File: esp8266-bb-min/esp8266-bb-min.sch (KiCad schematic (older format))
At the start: 14 parts, among them J1 Conn_01x02_Male, J2 Conn_02x08_Odd_Even, U1 tps77633d-SOIC8, U2 ESP-12F

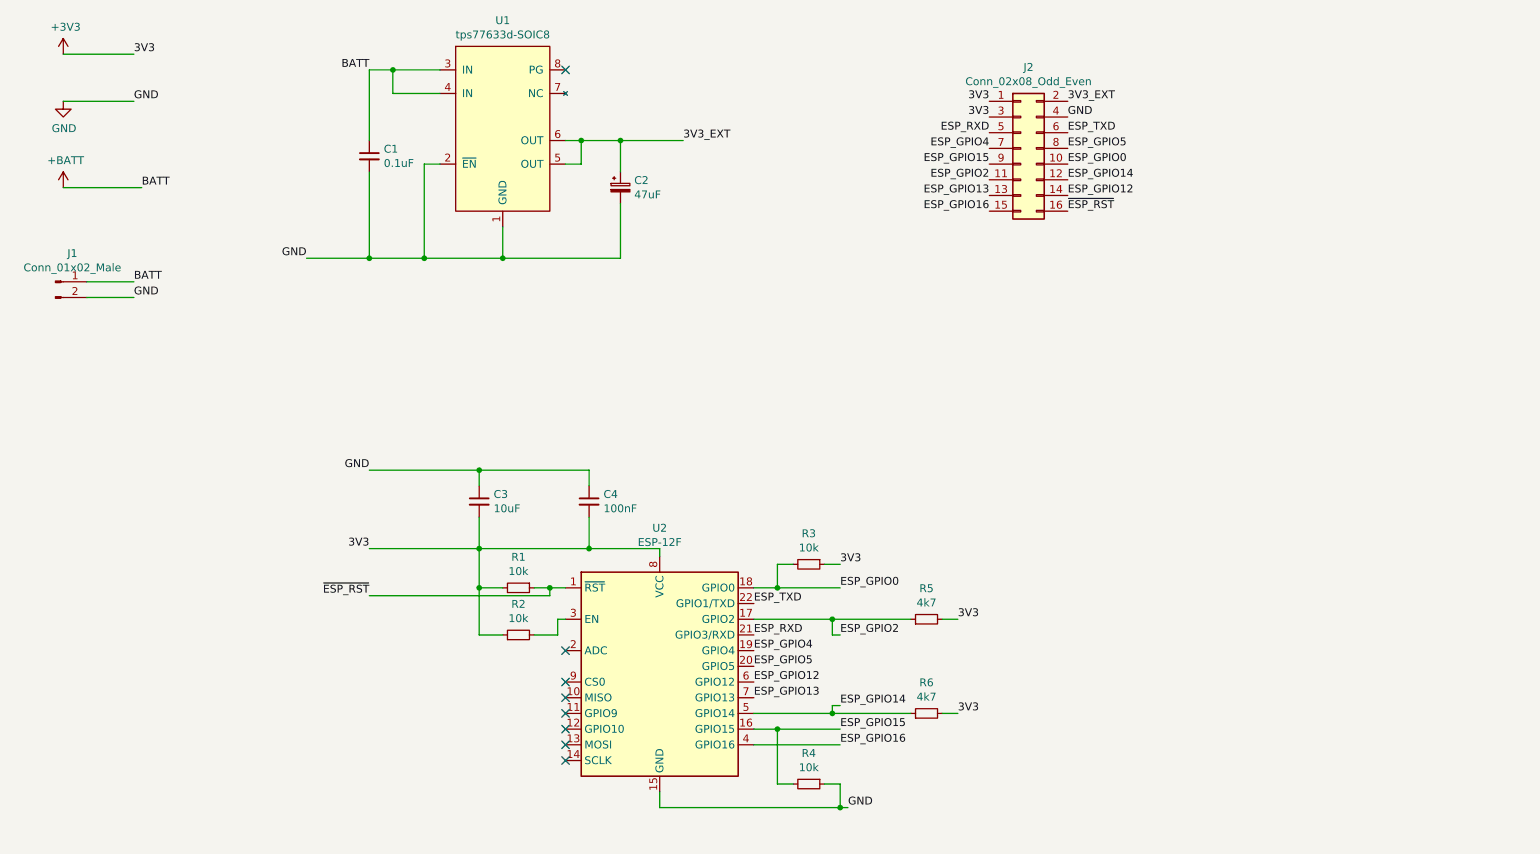
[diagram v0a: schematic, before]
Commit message: *: cleanup of erc errors
Signed-off-by: Dominik Laton <dominik.laton@web.de>
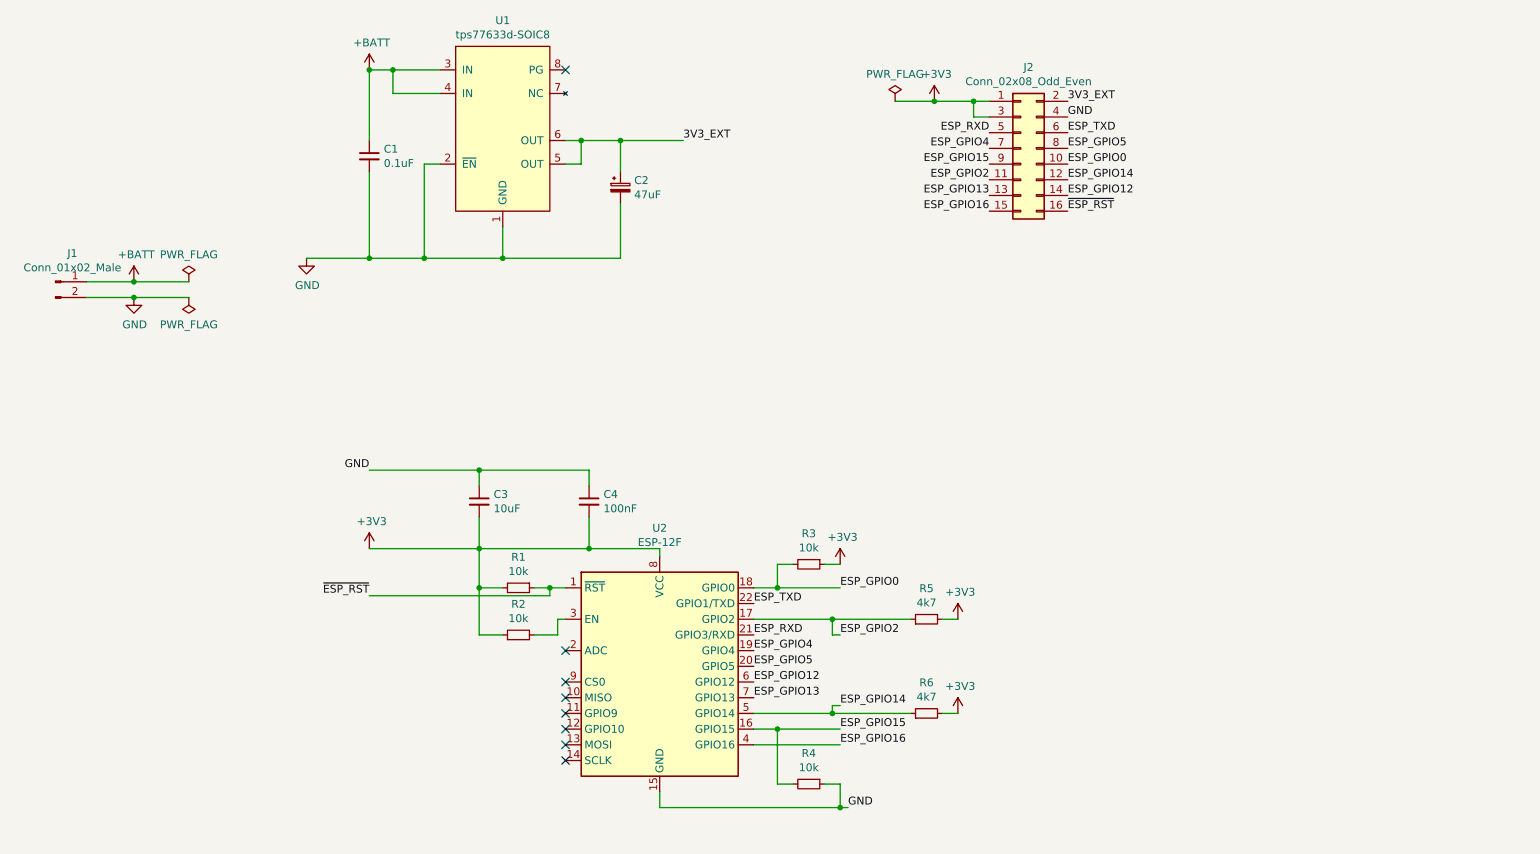
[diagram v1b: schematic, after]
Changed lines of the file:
@@
 L power:+3V3 #PWR0101
 U 1 1 5FA21016
-P 1050 850
-F 0 "#PWR0101" H 1050 700 50  0001 C CNN
-F 1 "+3V3" H 1065 1023 50  0000 C CNN
-F 2 "" H 1050 850 50  0001 C CNN
-F 3 "" H 1050 850 50  0001 C CNN
-	1    1050 850
+P 6600 1150
+F 0 "#PWR0101" H 6600 1000 50  0001 C CNN
+F 1 "+3V3" H 6615 1323 50  0000 C CNN
+F 2 "" H 6600 1150 50  0001 C CNN
+F 3 "" H 6600 1150 50  0001 C CNN
+	1    6600 1150
 	1    0    0    -1
 $EndComp
@@
 L power:GND #PWR0102
 U 1 1 5FA2192E
-P 1050 1150
-F 0 "#PWR0102" H 1050 900 50  0001 C CNN
-F 1 "GND" H 1055 977 50  0000 C CNN
-F 2 "" H 1050 1150 50  0001 C CNN
-F 3 "" H 1050 1150 50  0001 C CNN
-	1    1050 1150
+P 1500 2400
+F 0 "#PWR0102" H 1500 2150 50  0001 C CNN
+F 1 "GND" H 1505 2227 50  0000 C CNN
+F 2 "" H 1500 2400 50  0001 C CNN
+F 3 "" H 1500 2400 50  0001 C CNN
+	1    1500 2400
 	1    0    0    -1
 $EndComp
@@
 L power:+BATT #PWR0103
 U 1 1 5FA21D4E
-P 1050 1700
-F 0 "#PWR0103" H 1050 1550 50  0001 C CNN
-F 1 "+BATT" H 1065 1873 50  0000 C CNN
-F 2 "" H 1050 1700 50  0001 C CNN
-F 3 "" H 1050 1700 50  0001 C CNN
-	1    1050 1700
+P 1500 2300
+F 0 "#PWR0103" H 1500 2150 50  0001 C CNN
+F 1 "+BATT" H 1515 2473 50  0000 C CNN
+F 2 "" H 1500 2300 50  0001 C CNN
+F 3 "" H 1500 2300 50  0001 C CNN
+	1    1500 2300
 	1    0    0    -1
 $EndComp
@@
 Wire Wire Line
 	1200 2300 1500 2300
-Text Label 1500 2300 0    50   ~ 0
-BATT
-Wire Wire Line
-	1050 1700 1550 1700
-Text Label 1550 1700 0    50   ~ 0
-BATT
-Wire Wire Line
-	1050 1150 1500 1150
-Text Label 1500 1150 0    50   ~ 0
-GND
 Wire Wire Line
 	1200 2400 1500 2400
-Text Label 1500 2400 0    50   ~ 0
-GND
-Wire Wire Line
-	1050 850  1500 850
-Text Label 1500 850  0    50   ~ 0
-3V3
 Text Label 7450 1150 0    50   ~ 0
 3V3_EXT
-Text Label 6950 1150 2    50   ~ 0
-3V3
 $Comp
 L domi3006:tps77633d-SOIC8 U1
@@
 Wire Wire Line
 	3150 950  3000 950
-Text Label 3000 950  2    50   ~ 0
-BATT
 Wire Wire Line
 	3450 1550 3350 1550
@@
 	3350 2150 3000 2150
 Connection ~ 3350 2150
-Text Label 2600 2150 2    50   ~ 0
-GND
 $Comp
 L Device:C_Small C1
@@
 Wire Wire Line
 	4850 4000 4400 4000
-Text Label 3000 4000 2    50   ~ 0
-3V3
 $Comp
 L Device:R_Small R1
@@
 Wire Wire Line
 	5900 4100 6000 4100
-Text Label 6000 4100 0    50   ~ 0
-3V3
 Text Label 6000 4250 0    50   ~ 0
 ESP_GPIO0
@@
 Text Label 6950 1850 2    50   ~ 0
 ESP_GPIO16
-Text Label 6950 1250 2    50   ~ 0
-3V3
 Text Label 7450 1250 0    50   ~ 0
 GND
@@
 Wire Wire Line
 	6650 5050 6750 5050
-Text Label 6750 5050 0    50   ~ 0
-3V3
-Text Label 6750 4450 0    50   ~ 0
-3V3
+$Comp
+L power:+BATT #PWR0104
+U 1 1 5FA5E5E8
+P 3000 950
+F 0 "#PWR0104" H 3000 800 50  0001 C CNN
+F 1 "+BATT" H 3015 1123 50  0000 C CNN
+F 2 "" H 3000 950 50  0001 C CNN
+F 3 "" H 3000 950 50  0001 C CNN
+	1    3000 950
+	1    0    0    -1
+$EndComp
+Connection ~ 3000 950
+Wire Wire Line
+	6950 1150 6850 1150
+$Comp
+L power:+3V3 #PWR0105
+U 1 1 5FA6F2A6
+P 3000 4000
+F 0 "#PWR0105" H 3000 3850 50  0001 C CNN
+F 1 "+3V3" H 3015 4173 50  0000 C CNN
+F 2 "" H 3000 4000 50  0001 C CNN
+F 3 "" H 3000 4000 50  0001 C CNN
+	1    3000 4000
+	1    0    0    -1
+$EndComp
+$Comp
+L power:GND #PWR0106
+U 1 1 5FA72AF4
+P 2600 2150
+F 0 "#PWR0106" H 2600 1900 50  0001 C CNN
+F 1 "GND" H 2605 1977 50  0000 C CNN
+F 2 "" H 2600 2150 50  0001 C CNN
+F 3 "" H 2600 2150 50  0001 C CNN
+	1    2600 2150
+	1    0    0    -1
+$EndComp
+$Comp
+L power:PWR_FLAG #FLG0101
+U 1 1 5FA7DBB5
+P 6350 1150
+F 0 "#FLG0101" H 6350 1225 50  0001 C CNN
+F 1 "PWR_FLAG" H 6350 1323 50  0000 C CNN
+F 2 "" H 6350 1150 50  0001 C CNN
+F 3 "~" H 6350 1150 50  0001 C CNN
+	1    6350 1150
+	1    0    0    -1
+$EndComp
+Wire Wire Line
+	6350 1150 6600 1150
+Connection ~ 6600 1150
+$Comp
+L power:PWR_FLAG #FLG0102
+U 1 1 5FA82854
+P 1850 2300
+F 0 "#FLG0102" H 1850 2375 50  0001 C CNN
+F 1 "PWR_FLAG" H 1850 2473 50  0000 C CNN
+F 2 "" H 1850 2300 50  0001 C CNN
+F 3 "~" H 1850 2300 50  0001 C CNN
+	1    1850 2300
+	1    0    0    -1
+$EndComp
+Wire Wire Line
+	1500 2300 1850 2300
+Connection ~ 1500 2300
+$Comp
+L power:PWR_FLAG #FLG0103
+U 1 1 5FA8A406
+P 1850 2400
+F 0 "#FLG0103" H 1850 2475 50  0001 C CNN
+F 1 "PWR_FLAG" H 1850 2573 50  0000 C CNN
+F 2 "" H 1850 2400 50  0001 C CNN
+F 3 "~" H 1850 2400 50  0001 C CNN
+	1    1850 2400
+	-1   0    0    1
+$EndComp
+Wire Wire Line
+	1500 2400 1850 2400
+Connection ~ 1500 2400
+Wire Wire Line
+	6850 1150 6850 1250
+Wire Wire Line
+	6850 1250 6950 1250
+Connection ~ 6850 1150
+Wire Wire Line
+	6850 1150 6600 1150
+$Comp
+L power:+3V3 #PWR?
+U 1 1 5FA98897
+P 6750 4450
+F 0 "#PWR?" H 6750 4300 50  0001 C CNN
+F 1 "+3V3" H 6765 4623 50  0000 C CNN
+F 2 "" H 6750 4450 50  0001 C CNN
+F 3 "" H 6750 4450 50  0001 C CNN
+	1    6750 4450
+	1    0    0    -1
+$EndComp
+$Comp
+L power:+3V3 #PWR?
+U 1 1 5FA997BF
+P 6750 5050
+F 0 "#PWR?" H 6750 4900 50  0001 C CNN
+F 1 "+3V3" H 6765 5223 50  0000 C CNN
+F 2 "" H 6750 5050 50  0001 C CNN
+F 3 "" H 6750 5050 50  0001 C CNN
+	1    6750 5050
+	1    0    0    -1
+$EndComp
+$Comp
+L power:+3V3 #PWR?
+U 1 1 5FA99D69
+P 6000 4100
+F 0 "#PWR?" H 6000 3950 50  0001 C CNN
+F 1 "+3V3" H 6015 4273 50  0000 C CNN
+F 2 "" H 6000 4100 50  0001 C CNN
+F 3 "" H 6000 4100 50  0001 C CNN
+	1    6000 4100
+	1    0    0    -1
+$EndComp
 $EndSCHEMATC

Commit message: sch: addressed issue domi3006/esp8266-bb-min#3
Signed-off-by: Dominik Laton <dominik.laton@web.de>
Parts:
- removed U1: tps77633d-SOIC8, domi3006:SOIC-8, symbol domi3006:tps77633d-SOIC8
- added R7: 56k, Resistor_SMD:R_0805_2012Metric_Pad1.20x1.40mm_HandSolder, symbol Device:R_Small
- added U1: LP38693MP-3.3, Package_TO_SOT_SMD:SOT-223-5, symbol Regulator_Linear:LP38693MP-3.3
- C1: value 0.1uF -> 1uF
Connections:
- net +3V3: now also C2.1, U1.3 (OUT)
- net +BATT: now also R7.2, U1.1 (EN), U1.4 (IN)
- net 3V3_EXT: no longer names the net of J2.2 (Pin_2)
- net 3V3_EXT: no longer C2.1
- net GND renamed -BATT
- net -BATT: now also R7.1, U1.5 (GND)
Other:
- note added: "-BATT and GND should meet at ldo\nC1 should be placed near to IN (max. 1cm)"
- moved on the sheet: C1
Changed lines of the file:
@@
-$EndComp
-$Comp
-L power:GND #PWR0102
-U 1 1 5FA2192E
-P 1500 2400
-F 0 "#PWR0102" H 1500 2150 50  0001 C CNN
-F 1 "GND" H 1505 2227 50  0000 C CNN
-F 2 "" H 1500 2400 50  0001 C CNN
-F 3 "" H 1500 2400 50  0001 C CNN
-	1    1500 2400
-	1    0    0    -1
 $EndComp
 $Comp
@@
 Wire Wire Line
 	1200 2300 1500 2300
-Wire Wire Line
-	1200 2400 1500 2400
-Text Label 7450 1150 0    50   ~ 0
-3V3_EXT
-$Comp
-L domi3006:tps77633d-SOIC8 U1
-U 1 1 5FA2A8A4
-P 3850 800
-F 0 "U1" H 3850 965 50  0000 C CNN
-F 1 "tps77633d-SOIC8" H 3850 874 50  0000 C CNN
-F 2 "domi3006:SOIC-8" H 3850 850 50  0001 C CNN
-F 3 "" H 3850 850 50  0001 C CNN
-	1    3850 800
-	1    0    0    -1
-$EndComp
-Wire Wire Line
-	3450 950  3150 950
-Wire Wire Line
-	3450 1100 3150 1100
-Wire Wire Line
-	3150 1100 3150 950
-Connection ~ 3150 950
-Wire Wire Line
-	3150 950  3000 950
-Wire Wire Line
-	3450 1550 3350 1550
-Wire Wire Line
-	3350 1550 3350 2150
-Wire Wire Line
-	3350 2150 3850 2150
-Wire Wire Line
-	3850 2150 3850 1950
-Wire Wire Line
-	3350 2150 3000 2150
-Connection ~ 3350 2150
 $Comp
 L Device:C_Small C1
 U 1 1 5FA2D191
-P 3000 1500
-F 0 "C1" H 3092 1546 50  0000 L CNN
-F 1 "0.1uF" H 3092 1455 50  0000 L CNN
-F 2 "Capacitor_SMD:C_0805_2012Metric_Pad1.18x1.45mm_HandSolder" H 3000 1500 50  0001 C CNN
-F 3 "~" H 3000 1500 50  0001 C CNN
-	1    3000 1500
-	1    0    0    -1
-$EndComp
-Wire Wire Line
-	3000 1600 3000 2150
-Connection ~ 3000 2150
-Wire Wire Line
-	3000 2150 2600 2150
-Wire Wire Line
-	3000 1400 3000 950
-NoConn ~ 4250 950
-Wire Wire Line
-	4250 1400 4350 1400
-Wire Wire Line
-	4250 1550 4350 1550
-Wire Wire Line
-	4350 1550 4350 1400
-Connection ~ 4350 1400
-Wire Wire Line
-	4350 1400 4600 1400
-Text Label 5000 1400 0    50   ~ 0
-3V3_EXT
+P 3000 1750
+F 0 "C1" H 3092 1796 50  0000 L CNN
+F 1 "1uF" H 3092 1705 50  0000 L CNN
+F 2 "Capacitor_SMD:C_0805_2012Metric_Pad1.18x1.45mm_HandSolder" H 3000 1750 50  0001 C CNN
+F 3 "~" H 3000 1750 50  0001 C CNN
+	1    3000 1750
+	1    0    0    -1
+$EndComp
 $Comp
 L Device:CP_Small C2
@@
 $EndComp
 Wire Wire Line
-	3850 2150 4600 2150
-Wire Wire Line
 	4600 2150 4600 1800
-Connection ~ 3850 2150
 Wire Wire Line
 	4600 1600 4600 1400
-Connection ~ 4600 1400
-Wire Wire Line
-	4600 1400 5000 1400
 Wire Wire Line
 	4850 4050 4850 4000
@@
 L power:+BATT #PWR0104
 U 1 1 5FA5E5E8
-P 3000 950
-F 0 "#PWR0104" H 3000 800 50  0001 C CNN
-F 1 "+BATT" H 3015 1123 50  0000 C CNN
-F 2 "" H 3000 950 50  0001 C CNN
-F 3 "" H 3000 950 50  0001 C CNN
-	1    3000 950
-	1    0    0    -1
-$EndComp
-Connection ~ 3000 950
+P 2750 1400
+F 0 "#PWR0104" H 2750 1250 50  0001 C CNN
+F 1 "+BATT" H 2765 1573 50  0000 C CNN
+F 2 "" H 2750 1400 50  0001 C CNN
+F 3 "" H 2750 1400 50  0001 C CNN
+	1    2750 1400
+	1    0    0    -1
+$EndComp
 Wire Wire Line
 	6950 1150 6850 1150
@@
 	1    0    0    -1
 $EndComp
-$Comp
-L power:GND #PWR0106
-U 1 1 5FA72AF4
-P 2600 2150
-F 0 "#PWR0106" H 2600 1900 50  0001 C CNN
-F 1 "GND" H 2605 1977 50  0000 C CNN
-F 2 "" H 2600 2150 50  0001 C CNN
-F 3 "" H 2600 2150 50  0001 C CNN
-	1    2600 2150
-	1    0    0    -1
-$EndComp
-$Comp
-L power:PWR_FLAG #FLG0101
-U 1 1 5FA7DBB5
-P 6350 1150
-F 0 "#FLG0101" H 6350 1225 50  0001 C CNN
-F 1 "PWR_FLAG" H 6350 1323 50  0000 C CNN
-F 2 "" H 6350 1150 50  0001 C CNN
-F 3 "~" H 6350 1150 50  0001 C CNN
-	1    6350 1150
-	1    0    0    -1
-$EndComp
-Wire Wire Line
-	6350 1150 6600 1150
-Connection ~ 6600 1150
 $Comp
 L power:PWR_FLAG #FLG0102
@@
 $EndComp
 Wire Wire Line
-	1500 2400 1850 2400
-Connection ~ 1500 2400
-Wire Wire Line
 	6850 1150 6850 1250
 Wire Wire Line
@@
 	6850 1150 6600 1150
 $Comp
-L power:+3V3 #PWR?
+L power:+3V3 #PWR0102
 U 1 1 5FA98897
 P 6750 4450
-F 0 "#PWR?" H 6750 4300 50  0001 C CNN
+F 0 "#PWR0102" H 6750 4300 50  0001 C CNN
 F 1 "+3V3" H 6765 4623 50  0000 C CNN
 F 2 "" H 6750 4450 50  0001 C CNN
@@
 $EndComp
 $Comp
-L power:+3V3 #PWR?
+L power:+3V3 #PWR0106
 U 1 1 5FA997BF
 P 6750 5050
-F 0 "#PWR?" H 6750 4900 50  0001 C CNN
+F 0 "#PWR0106" H 6750 4900 50  0001 C CNN
 F 1 "+3V3" H 6765 5223 50  0000 C CNN
 F 2 "" H 6750 5050 50  0001 C CNN
@@
 $EndComp
 $Comp
-L power:+3V3 #PWR?
+L power:+3V3 #PWR0107
 U 1 1 5FA99D69
 P 6000 4100
-F 0 "#PWR?" H 6000 3950 50  0001 C CNN
+F 0 "#PWR0107" H 6000 3950 50  0001 C CNN
 F 1 "+3V3" H 6015 4273 50  0000 C CNN
 F 2 "" H 6000 4100 50  0001 C CNN
@@
 	1    0    0    -1
 $EndComp
+$Comp
+L Regulator_Linear:LP38693MP-3.3 U1
+U 1 1 5FC250F2
+P 4000 1500
+F 0 "U1" H 4000 1842 50  0000 C CNN
+F 1 "LP38693MP-3.3" H 4000 1751 50  0000 C CNN
+F 2 "Package_TO_SOT_SMD:SOT-223-5" H 4000 1500 50  0001 C CNN
+F 3 "https://www.ti.com/lit/ds/symlink/lp38693.pdf" H 4000 1500 50  0001 C CNN
+	1    4000 1500
+	1    0    0    -1
+$EndComp
+Wire Wire Line
+	4400 1400 4600 1400
+Wire Wire Line
+	3000 1850 3000 2150
+Wire Wire Line
+	3600 1400 3400 1400
+Wire Wire Line
+	3000 1400 3000 1650
+Wire Wire Line
+	3000 2150 3400 2150
+Wire Wire Line
+	4000 1800 4000 2150
+Connection ~ 4000 2150
+Wire Wire Line
+	4000 2150 4600 2150
+Wire Wire Line
+	4600 2150 4600 2250
+Connection ~ 4600 2150
+$Comp
+L power:GND #PWR0108
+U 1 1 5FC3E3A8
+P 4600 2250
+F 0 "#PWR0108" H 4600 2000 50  0001 C CNN
+F 1 "GND" H 4605 2077 50  0000 C CNN
+F 2 "" H 4600 2250 50  0001 C CNN
+F 3 "" H 4600 2250 50  0001 C CNN
+	1    4600 2250
+	1    0    0    -1
+$EndComp
+$Comp
+L power:-BATT #PWR0109
+U 1 1 5FC40056
+P 2750 2150
+F 0 "#PWR0109" H 2750 2000 50  0001 C CNN
+F 1 "-BATT" H 2765 2323 50  0000 C CNN
+F 2 "" H 2750 2150 50  0001 C CNN
+F 3 "" H 2750 2150 50  0001 C CNN
+	1    2750 2150
+	1    0    0    -1
+$EndComp
+Wire Wire Line
+	2750 2150 3000 2150
+Connection ~ 3000 2150
+Wire Wire Line
+	2750 1400 3000 1400
+Connection ~ 3000 1400
+$Comp
+L Device:R_Small R7
+U 1 1 5FC4664C
+P 3400 1750
+F 0 "R7" V 3204 1750 50  0000 C CNN
+F 1 "56k" V 3295 1750 50  0000 C CNN
+F 2 "Resistor_SMD:R_0805_2012Metric_Pad1.20x1.40mm_HandSolder" H 3400 1750 50  0001 C CNN
+F 3 "~" H 3400 1750 50  0001 C CNN
+	1    3400 1750
+	-1   0    0    1
+$EndComp
+Wire Wire Line
+	3600 1500 3400 1500
+Wire Wire Line
+	3400 1500 3400 1400
+Connection ~ 3400 1400
+Wire Wire Line
+	3400 1400 3000 1400
+Wire Wire Line
+	3400 1500 3400 1650
+Connection ~ 3400 1500
+Wire Wire Line
+	3400 1850 3400 2150
+Connection ~ 3400 2150
+Wire Wire Line
+	3400 2150 4000 2150
+$Comp
+L power:+3.3V #PWR0110
+U 1 1 5FC51A47
+P 4800 1400
+F 0 "#PWR0110" H 4800 1250 50  0001 C CNN
+F 1 "+3.3V" H 4815 1573 50  0000 C CNN
+F 2 "" H 4800 1400 50  0001 C CNN
+F 3 "" H 4800 1400 50  0001 C CNN
+	1    4800 1400
+	1    0    0    -1
+$EndComp
+Wire Wire Line
+	4600 1400 4800 1400
+Connection ~ 4600 1400
+NoConn ~ 7450 1150
+Wire Wire Line
+	1200 2400 1650 2400
+$Comp
+L power:-BATT #PWR0111
+U 1 1 5FC561B1
+P 1650 2400
+F 0 "#PWR0111" H 1650 2250 50  0001 C CNN
+F 1 "-BATT" H 1665 2573 50  0000 C CNN
+F 2 "" H 1650 2400 50  0001 C CNN
+F 3 "" H 1650 2400 50  0001 C CNN
+	1    1650 2400
+	1    0    0    -1
+$EndComp
+Connection ~ 1650 2400
+Wire Wire Line
+	1650 2400 1850 2400
+Text Notes 2700 2350 0    50   ~ 0
+-BATT and GND should meet at ldo\nC1 should be placed near to IN (max. 1cm)
 $EndSCHEMATC
